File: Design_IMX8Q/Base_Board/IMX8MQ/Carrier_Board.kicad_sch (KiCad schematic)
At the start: 1 part, among them U14 IMX6ModuleConector_300

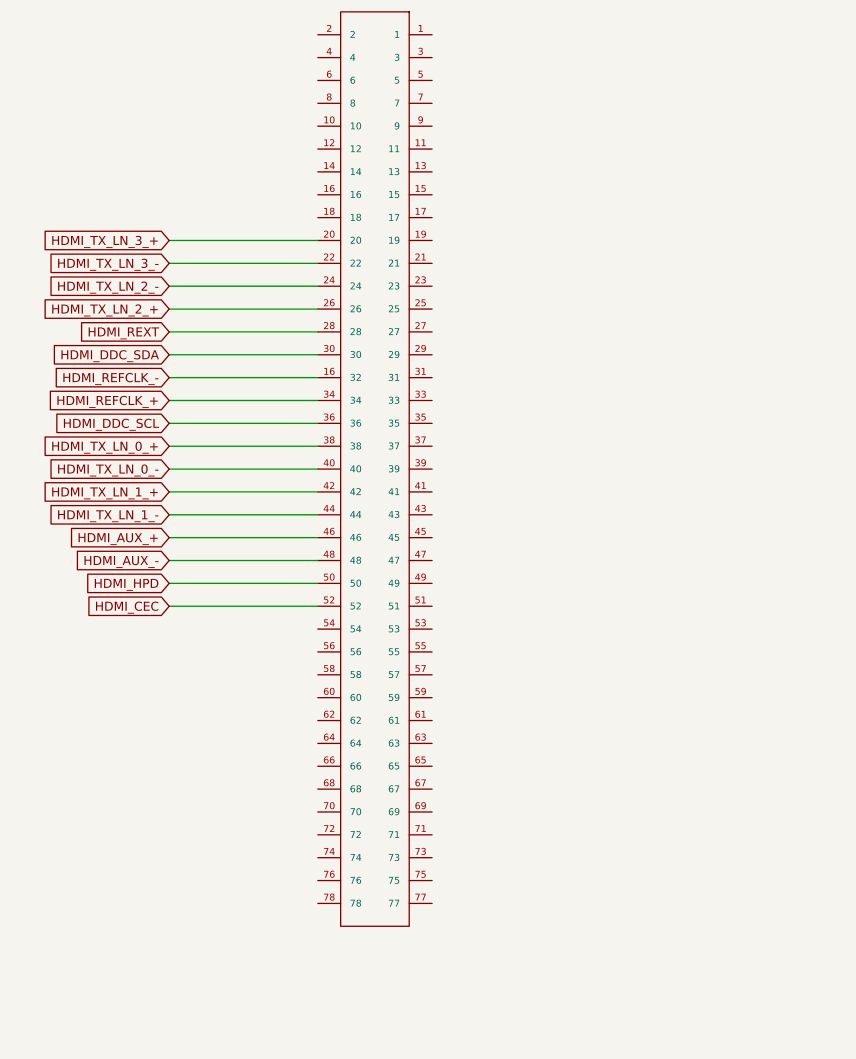
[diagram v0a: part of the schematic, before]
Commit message: Add QSPI and more color
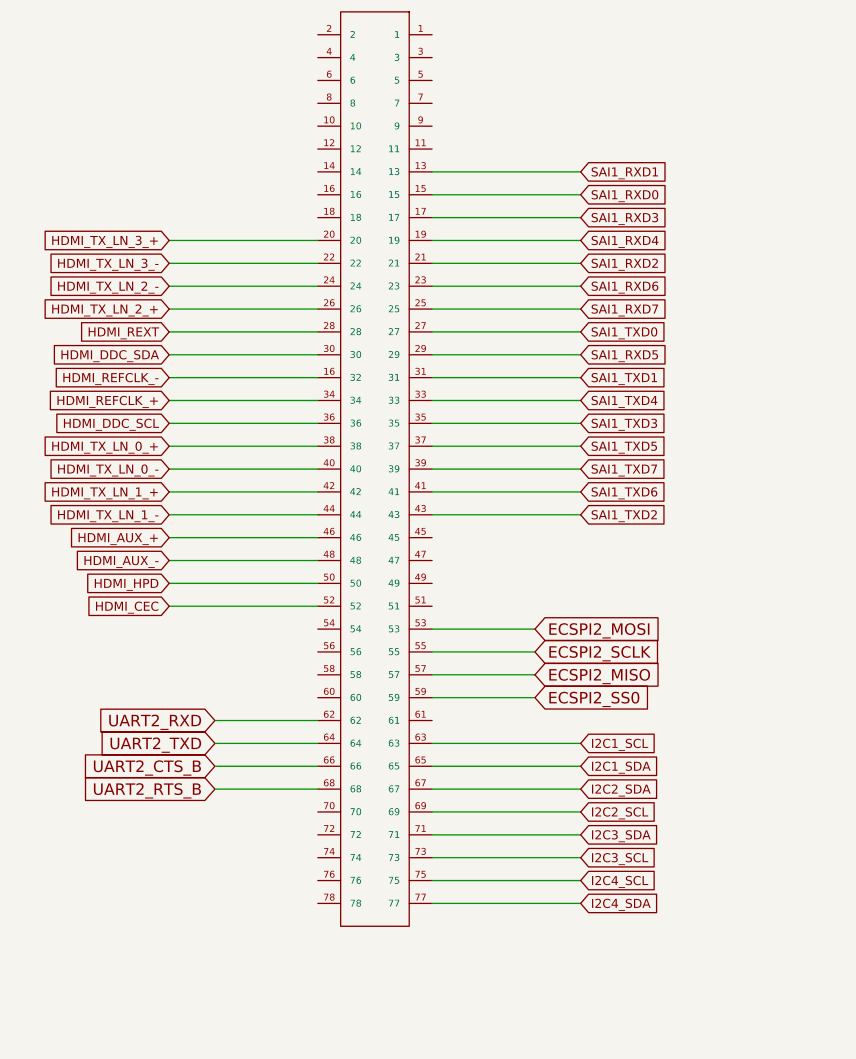
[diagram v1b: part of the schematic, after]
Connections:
- net SAI1_RXD1: now reaches U14.13
- net SAI1_RXD0: now reaches U14.15
- net SAI1_RXD3: now reaches U14.17
- net SAI1_RXD4: now reaches U14.19
- net SAI1_RXD2: now reaches U14.21
- net SAI1_RXD6: now reaches U14.23
- net SAI1_RXD7: now reaches U14.25
- net SAI1_TXD0: now reaches U14.27
- net SAI1_RXD5: now reaches U14.29
- net SAI1_TXD1: now reaches U14.31
- net SAI1_TXD4: now reaches U14.33
- net SAI1_TXD3: now reaches U14.35
- net SAI1_TXD5: now reaches U14.37
- net SAI1_TXD7: now reaches U14.39
- net SAI1_TXD6: now reaches U14.41
- net SAI1_TXD2: now reaches U14.43
- net ECSPI2_MOSI: now reaches U14.53
- net ECSPI2_SCLK: now reaches U14.55
- net ECSPI2_MISO: now reaches U14.57
- net ECSPI2_SS0: now reaches U14.59
- net UART2_RXD: now reaches U14.62
- net I2C1_SCL: now reaches U14.63
- net UART2_TXD: now reaches U14.64
- net I2C1_SDA: now reaches U14.65
- net UART2_CTS_B: now reaches U14.66
- net I2C2_SDA: now reaches U14.67
- net UART2_RTS_B: now reaches U14.68
- net I2C2_SCL: now reaches U14.69
- net I2C3_SDA: now reaches U14.71
- net I2C3_SCL: now reaches U14.73
- net I2C4_SCL: now reaches U14.75
- net I2C4_SDA: now reaches U14.77

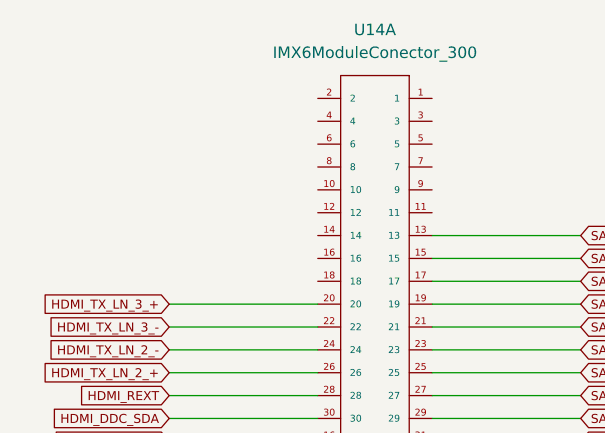
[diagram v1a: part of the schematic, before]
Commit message: it was inserted power control system
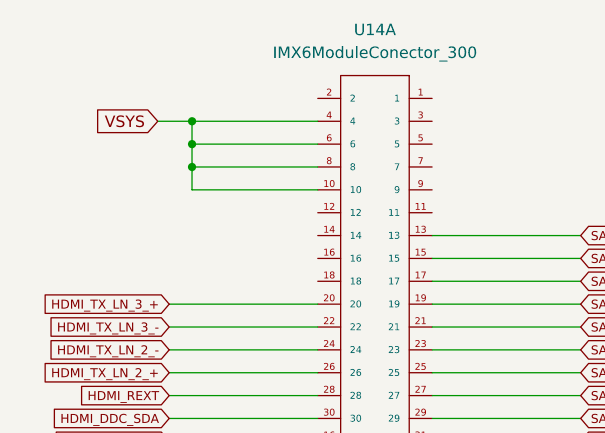
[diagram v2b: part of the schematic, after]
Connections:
- net VSYS: now reaches U14.10
- net VSYS: now also U14.4, U14.6, U14.8
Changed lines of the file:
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@@
 (kicad_sch (version 20230121) (generator eeschema)
   (paper "A4")
+  (junction (at -91.44 35.56) (diameter 0) (color 0 0 0 0)
+  )
+  (junction (at -91.44 38.1) (diameter 0) (color 0 0 0 0)
+  )
+  (junction (at -91.44 40.64) (diameter 0) (color 0 0 0 0)
+  )
   (wire (pts (xy -77.47 78.74) (xy -93.98 78.74))
     (stroke (width 0) (type default))
@@
     (stroke (width 0) (type default))
   )
+  (wire (pts (xy -91.44 35.56) (xy -91.44 38.1))
+    (stroke (width 0) (type default))
+  )
   (wire (pts (xy 250.19 115.57) (xy 233.68 115.57))
     (stroke (width 0) (type default))
@@
     (stroke (width 0) (type default))
   )
+  (wire (pts (xy -91.44 38.1) (xy -77.47 38.1))
+    (stroke (width 0) (type default))
+  )
   (wire (pts (xy -64.77 66.04) (xy -48.26 66.04))
     (stroke (width 0) (type default))
@@
     (stroke (width 0) (type default))
   )
+  (wire (pts (xy -91.44 38.1) (xy -91.44 40.64))
+    (stroke (width 0) (type default))
+  )
   (wire (pts (xy -64.77 81.28) (xy -48.26 81.28))
     (stroke (width 0) (type default))
@@
     (stroke (width 0) (type default))
   )
+  (wire (pts (xy -77.47 43.18) (xy -91.44 43.18))
+    (stroke (width 0) (type default))
+  )
   (wire (pts (xy 168.91 99.06) (xy 152.4 99.06))
     (stroke (width 0) (type default))
@@
     (stroke (width 0) (type default))
   )
+  (wire (pts (xy -91.44 35.56) (xy -77.47 35.56))
+    (stroke (width 0) (type default))
+  )
   (wire (pts (xy 110.49 63.5) (xy 93.98 63.5))
     (stroke (width 0) (type default))
@@
     (stroke (width 0) (type default))
   )
+  (wire (pts (xy -95.25 35.56) (xy -91.44 35.56))
+    (stroke (width 0) (type default))
+  )
   (wire (pts (xy 110.49 60.96) (xy 93.98 60.96))
     (stroke (width 0) (type default))
   )
+  (wire (pts (xy -91.44 40.64) (xy -91.44 43.18))
+    (stroke (width 0) (type default))
+  )
   (wire (pts (xy -64.77 71.12) (xy -48.26 71.12))
     (stroke (width 0) (type default))
@@
   )
   (wire (pts (xy -77.47 88.9) (xy -93.98 88.9))
+    (stroke (width 0) (type default))
+  )
+  (wire (pts (xy -91.44 40.64) (xy -77.47 40.64))
     (stroke (width 0) (type default))
   )
@@
       (effects (font (size 1.27 1.27)) (justify right) hide)
     )
+  )
+  (global_label "VSYS" (shape input) (at -95.25 35.56 180) (fields_autoplaced)
+    (effects (font (size 1.27 1.27)) (justify right))
+    (property "Intersheetrefs" "${INTERSHEET_REFS}" (at -102.752 35.56 0)
+      (effects (font (size 1.27 1.27)) (justify right) hide)
+    )
